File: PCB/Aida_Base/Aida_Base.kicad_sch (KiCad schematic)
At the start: 228 parts, among them J1 AudioJack4, J10 Conn_01x03_Pin, J11 Conn_01x04_Pin, J12 Conn_01x04_Pin, J13 Conn_01x04_Pin, J14 Conn_01x04_Pin, J15 Conn_01x04_Pin, J16 Conn_01x04_Pin, J17 Conn_02x02_Odd_Even, J18 Conn_02x02_Odd_Even, J19 Conn_01x04_Pin, J2 AudioJack4, J20 Conn_01x06_Pin, J21 Conn_01x06_Pin, J22 Conn_01x04_Pin, J3 USB_C_Receptacle_L, J4 USB_C_Receptacle_R, J5 Conn_01x02_Pin, J6 Conn_01x02_Pin, J7 Conn_01x05_Pin, J8 Conn_01x05_Pin, J9 Conn_01x03_Pin, Q1 BSS138, Q2 BSS138, SW1 BOOT, SW2 BOOT, SW3 RESET, SW4 RESET, U3 RP2040_L, U4 RP2040_R, U5 W25Q128JVS, U6 W25Q128JVS, U7 AP2112K-3.3, U8 AP2112K-3.3, Y1 12MHz, Y2 12MHz

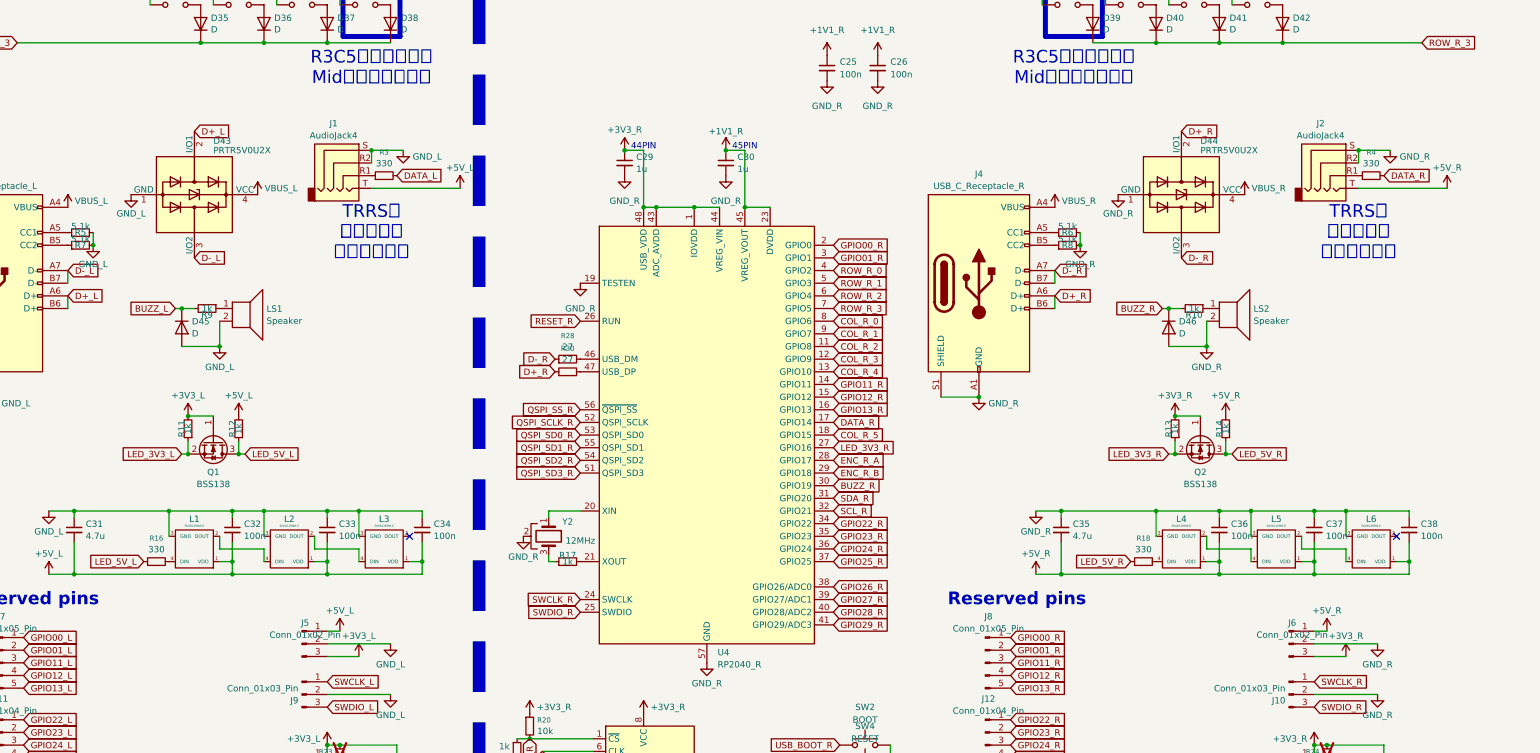
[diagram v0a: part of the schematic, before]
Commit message: 左手側配線。ほぼ完了。
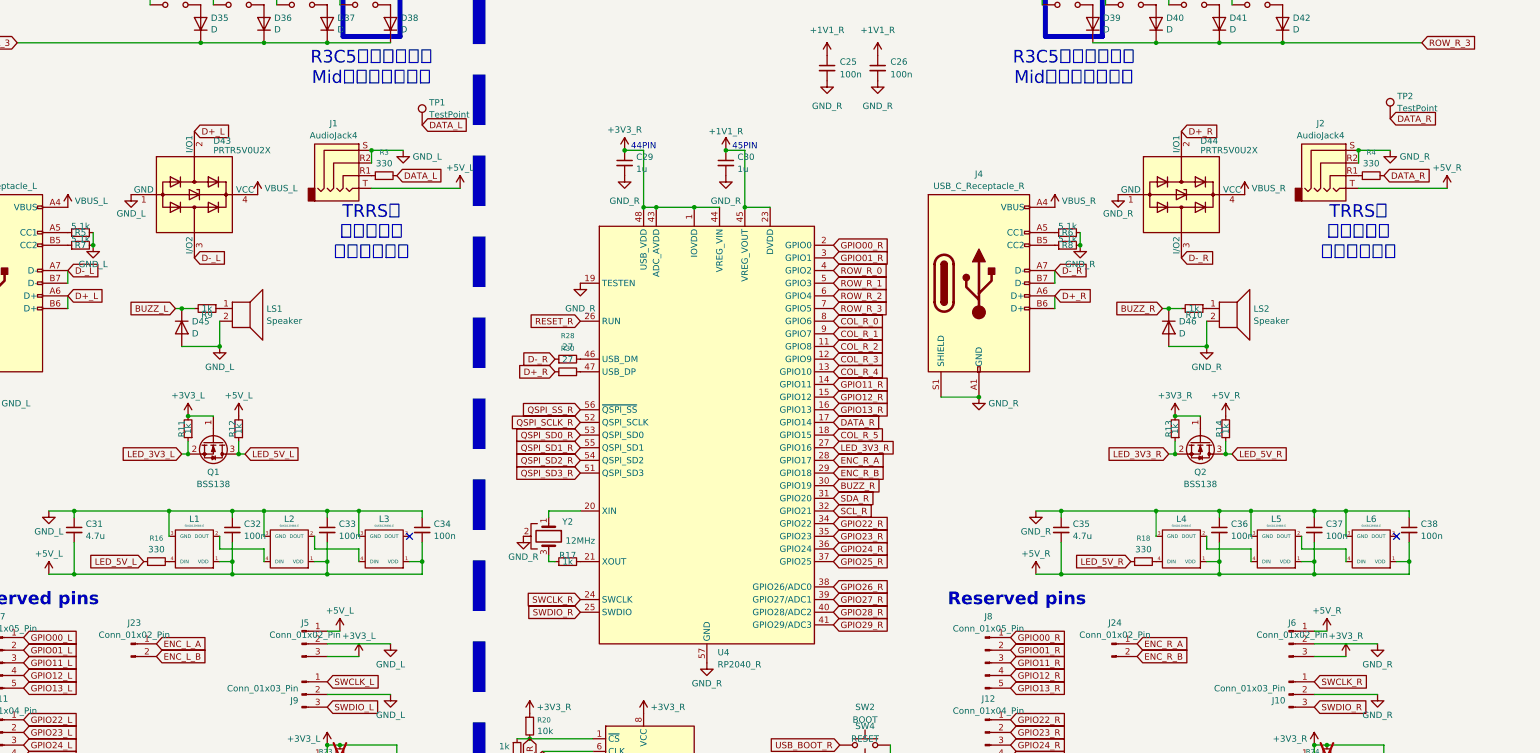
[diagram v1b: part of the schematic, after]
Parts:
- added J23, J24: Conn_01x02_Pin, Connector_PinHeader_2.00mm:PinHeader_1x02_P2.00mm_Vertical, symbol Connector:Conn_01x02_Pin
- added TP1, TP2: TestPoint, Connector_PinHeader_2.00mm:PinHeader_1x01_P2.00mm_Vertical, symbol Connector:TestPoint
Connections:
- net DATA_L: now also TP1.1
- net DATA_R: now also TP2.1
- net ENC_L_A: now also J23.1 (Pin_1)
- net ENC_L_B: now also J23.2 (Pin_2)
- net ENC_R_A: now also J24.1 (Pin_1)
- net ENC_R_B: now also J24.2 (Pin_2)

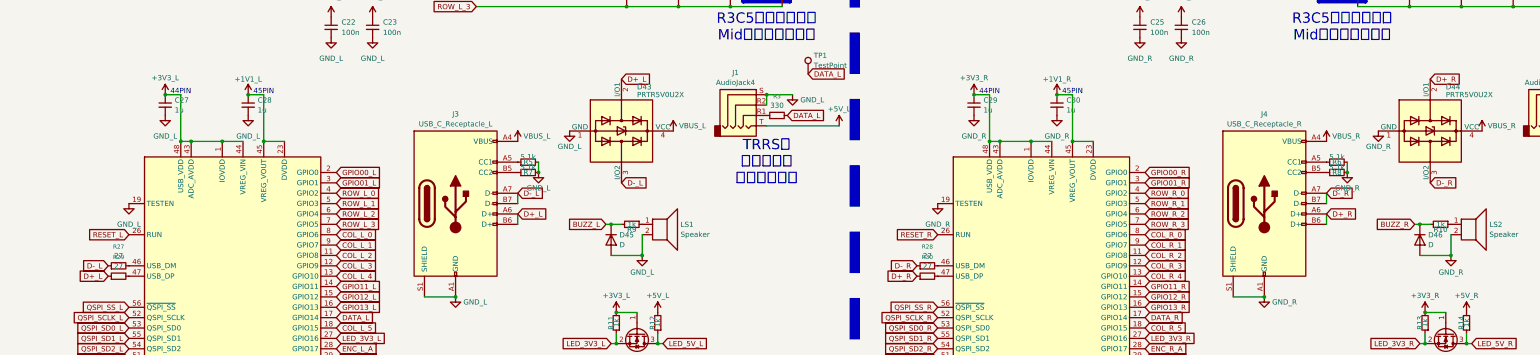
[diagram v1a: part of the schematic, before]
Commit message: ボトムプレートの穴あけ用に、左手側パーツ配置調整。
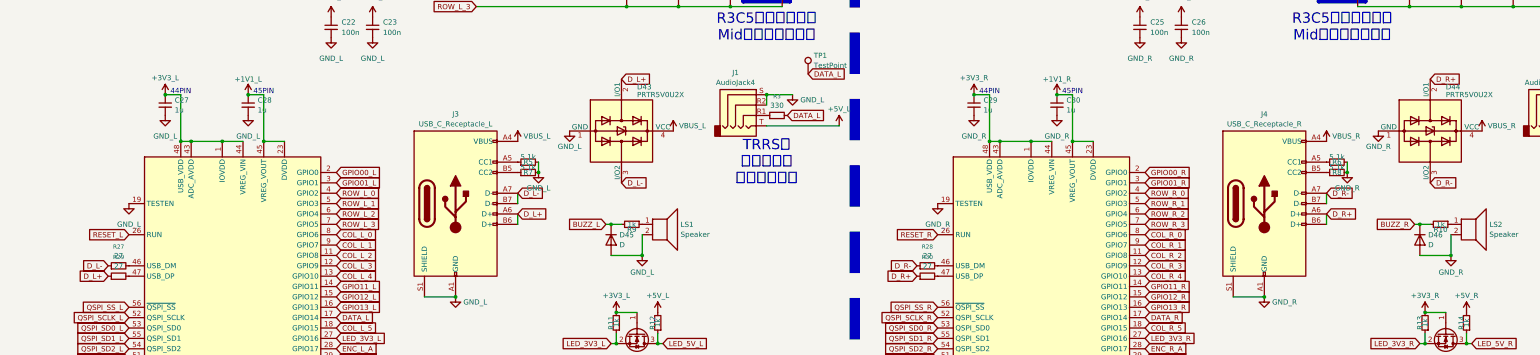
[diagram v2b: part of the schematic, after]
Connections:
- net D+_L renamed D_L+
- net D+_R renamed D_R+
- net D-_L renamed D_L-
- net D-_R renamed D_R-
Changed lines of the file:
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@@
 		)
 	)
-	(global_label "D+_R"
+	(global_label "D_R+"
 		(shape input)
 		(at 322.58 133.35 0)
@@
 		)
 	)
-	(global_label "D-_R"
+	(global_label "D_R-"
 		(shape input)
 		(at 322.58 128.27 0)
@@
 		)
 	)
-	(global_label "D-_L"
+	(global_label "D_L-"
 		(shape input)
 		(at 149.86 125.73 0)
@@
 		)
 	)
-	(global_label "D+_R"
+	(global_label "D_R+"
 		(shape input)
 		(at 347.98 100.33 0)
@@
 		)
 	)
-	(global_label "D-_L"
+	(global_label "D_L-"
 		(shape input)
 		(at 24.13 146.05 180)
@@
 		)
 	)
-	(global_label "D+_L"
+	(global_label "D_L+"
 		(shape input)
 		(at 149.86 100.33 0)
@@
 		)
 	)
-	(global_label "D+_L"
+	(global_label "D_L+"
 		(shape input)
 		(at 24.13 148.59 180)
@@
 		)
 	)
-	(global_label "D+_R"
+	(global_label "D_R+"
 		(shape input)
 		(at 222.25 148.59 180)
@@
 		)
 	)
-	(global_label "D-_R"
+	(global_label "D_R-"
 		(shape input)
 		(at 222.25 146.05 180)
@@
 		)
 	)
-	(global_label "D+_L"
+	(global_label "D_L+"
 		(shape input)
 		(at 124.46 133.35 0)
@@
 		)
 	)
-	(global_label "D-_L"
+	(global_label "D_L-"
 		(shape input)
 		(at 124.46 128.27 0)
@@
 		)
 	)
-	(global_label "D-_R"
+	(global_label "D_R-"
 		(shape input)
 		(at 347.98 125.73 0)

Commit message: 右手パーツ配置中。MCUまわりきびしい
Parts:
- D7: now not fitted
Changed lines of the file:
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@@
 		(exclude_from_sim no)
 		(in_bom yes)
-		(on_board yes)
-		(dnp no)
+		(on_board no)
+		(dnp yes)
 		(property "Reference" "D7"
 			(at 328.422 39.4716 90)

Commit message: 右手パーツ配置中
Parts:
- H_btm_L3, H_btm_L4, H_btm_L5, H_btm_L6: value MountingHole -> GND_L
- H_btm_R3, H_btm_R4, H_btm_R5, H_btm_R6: value MountingHole -> GND_R
- H_mid_L1, H_mid_L2: value MountingHole -> GND_L_to_Mid
- H_mid_R1, H_mid_R2: value MountingHole -> GND_R_to_Mid
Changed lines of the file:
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@@
 			)
 		)
-		(property "Value" "MountingHole"
+		(property "Value" "GND_R"
 			(at 217.17 276.733 0)
 			(effects
@@
 			)
 		)
-		(property "Value" "MountingHole"
+		(property "Value" "GND_L_to_Mid"
 			(at 73.66 267.843 0)
 			(effects
@@
 			)
 		)
-		(property "Value" "MountingHole"
+		(property "Value" "GND_L"
 			(at 41.91 276.733 0)
 			(effects
@@
 			)
 		)
-		(property "Value" "MountingHole"
+		(property "Value" "GND_L"
 			(at 21.59 271.653 0)
 			(effects
@@
 			)
 		)
-		(property "Value" "MountingHole"
+		(property "Value" "GND_R_to_Mid"
 			(at 271.78 267.843 0)
 			(effects
@@
 			)
 		)
-		(property "Value" "MountingHole"
+		(property "Value" "GND_L"
 			(at 19.05 276.733 0)
 			(effects
@@
 			)
 		)
-		(property "Value" "MountingHole"
+		(property "Value" "GND_R"
 			(at 237.49 271.653 0)
 			(effects
@@
 			)
 		)
-		(property "Value" "MountingHole"
+		(property "Value" "GND_R"
 			(at 240.03 276.733 0)
 			(effects
@@
 			)
 		)
-		(property "Value" "MountingHole"
+		(property "Value" "GND_L_to_Mid"
 			(at 90.17 267.843 0)
 			(effects
@@
 			)
 		)
-		(property "Value" "MountingHole"
+		(property "Value" "GND_L"
 			(at 39.37 271.653 0)
 			(effects
@@
 			)
 		)
-		(property "Value" "MountingHole"
+		(property "Value" "GND_R_to_Mid"
 			(at 288.29 267.843 0)
 			(effects
@@
 			)
 		)
-		(property "Value" "MountingHole"
+		(property "Value" "GND_R"
 			(at 219.71 271.653 0)
 			(effects

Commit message: ソケットの3Dモデルを、1.2ｍｍ厚のPCBに合わせて位置調整。
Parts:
- SW_-1, SW_/1, SW_<1, SW_>1, SW_A1, SW_B1, SW_BS1, SW_C1, SW_CMD_L1, SW_CMD_R1, SW_CTL1, SW_D1, SW_E1, SW_ENT1, SW_F1, SW_I1, SW_J1, SW_K1, SW_L1, SW_M1, SW_N1, SW_O1, SW_OPT_L1, SW_OPT_R1, SW_S1, SW_SPC1, SW_V1, SW_W1, SW_X1, SW_Z1: footprint Lib_Local:Kailh_socket_ChocV2 -> Lib_Local:Kailh_socket_ChocV2_for_T=1.2mmPCB
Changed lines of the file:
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@@
 			)
 		)
-		(property "Footprint" "Lib_Local:Kailh_socket_ChocV2"
+		(property "Footprint" "Lib_Local:Kailh_socket_ChocV2_for_T=1.2mmPCB"
 			(at 146.05 57.15 0)
 			(effects
@@
 			)
 		)
-		(property "Footprint" "Lib_Local:Kailh_socket_ChocV2"
+		(property "Footprint" "Lib_Local:Kailh_socket_ChocV2_for_T=1.2mmPCB"
 			(at 363.22 31.75 0)
 			(effects
@@
 			)
 		)
-		(property "Footprint" "Lib_Local:Kailh_socket_ChocV2"
+		(property "Footprint" "Lib_Local:Kailh_socket_ChocV2_for_T=1.2mmPCB"
 			(at 146.05 44.45 0)
 			(effects
@@
 			)
 		)
-		(property "Footprint" "Lib_Local:Kailh_socket_ChocV2"
+		(property "Footprint" "Lib_Local:Kailh_socket_ChocV2_for_T=1.2mmPCB"
 			(at 171.45 57.15 0)
 			(effects
@@
 			)
 		)
-		(property "Footprint" "Lib_Local:Kailh_socket_ChocV2"
+		(property "Footprint" "Lib_Local:Kailh_socket_ChocV2_for_T=1.2mmPCB"
 			(at 388.62 57.15 0)
 			(effects
@@
 			)
 		)
-		(property "Footprint" "Lib_Local:Kailh_socket_ChocV2"
+		(property "Footprint" "Lib_Local:Kailh_socket_ChocV2_for_T=1.2mmPCB"
 			(at 388.62 44.45 0)
 			(effects
@@
 			)
 		)
-		(property "Footprint" "Lib_Local:Kailh_socket_ChocV2"
+		(property "Footprint" "Lib_Local:Kailh_socket_ChocV2_for_T=1.2mmPCB"
 			(at 146.05 31.75 0)
 			(effects
@@
 			)
 		)
-		(property "Footprint" "Lib_Local:Kailh_socket_ChocV2"
+		(property "Footprint" "Lib_Local:Kailh_socket_ChocV2_for_T=1.2mmPCB"
 			(at 146.05 69.85 0)
 			(effects
@@
 			)
 		)
-		(property "Footprint" "Lib_Local:Kailh_socket_ChocV2"
+		(property "Footprint" "Lib_Local:Kailh_socket_ChocV2_for_T=1.2mmPCB"
 			(at 363.22 69.85 0)
 			(effects
@@
 			)
 		)
-		(property "Footprint" "Lib_Local:Kailh_socket_ChocV2"
+		(property "Footprint" "Lib_Local:Kailh_socket_ChocV2_for_T=1.2mmPCB"
 			(at 171.45 69.85 0)
 			(effects
@@
 			)
 		)
-		(property "Footprint" "Lib_Local:Kailh_socket_ChocV2"
+		(property "Footprint" "Lib_Local:Kailh_socket_ChocV2_for_T=1.2mmPCB"
 			(at 337.82 57.15 0)
 			(effects
@@
 			)
 		)
-		(property "Footprint" "Lib_Local:Kailh_socket_ChocV2"
+		(property "Footprint" "Lib_Local:Kailh_socket_ChocV2_for_T=1.2mmPCB"
 			(at 363.22 57.15 0)
 			(effects
@@
 			)
 		)
-		(property "Footprint" "Lib_Local:Kailh_socket_ChocV2"
+		(property "Footprint" "Lib_Local:Kailh_socket_ChocV2_for_T=1.2mmPCB"
 			(at 184.15 69.85 0)
 			(effects
@@
 			)
 		)
-		(property "Footprint" "Lib_Local:Kailh_socket_ChocV2"
+		(property "Footprint" "Lib_Local:Kailh_socket_ChocV2_for_T=1.2mmPCB"
 			(at 158.75 69.85 0)
 			(effects
@@
 			)
 		)
-		(property "Footprint" "Lib_Local:Kailh_socket_ChocV2"
+		(property "Footprint" "Lib_Local:Kailh_socket_ChocV2_for_T=1.2mmPCB"
 			(at 363.22 44.45 0)
 			(effects
@@
 			)
 		)
-		(property "Footprint" "Lib_Local:Kailh_socket_ChocV2"
+		(property "Footprint" "Lib_Local:Kailh_socket_ChocV2_for_T=1.2mmPCB"
 			(at 133.35 31.75 0)
 			(effects
@@
 			)
 		)
-		(property "Footprint" "Lib_Local:Kailh_socket_ChocV2"
+		(property "Footprint" "Lib_Local:Kailh_socket_ChocV2_for_T=1.2mmPCB"
 			(at 350.52 69.85 0)
 			(effects
@@
 			)
 		)
-		(property "Footprint" "Lib_Local:Kailh_socket_ChocV2"
+		(property "Footprint" "Lib_Local:Kailh_socket_ChocV2_for_T=1.2mmPCB"
 			(at 375.92 57.15 0)
 			(effects
@@
 			)
 		)
-		(property "Footprint" "Lib_Local:Kailh_socket_ChocV2"
+		(property "Footprint" "Lib_Local:Kailh_socket_ChocV2_for_T=1.2mmPCB"
 			(at 350.52 57.15 0)
 			(effects
@@
 			)
 		)
-		(property "Footprint" "Lib_Local:Kailh_socket_ChocV2"
+		(property "Footprint" "Lib_Local:Kailh_socket_ChocV2_for_T=1.2mmPCB"
 			(at 120.65 44.45 0)
 			(effects
@@
 			)
 		)
-		(property "Footprint" "Lib_Local:Kailh_socket_ChocV2"
+		(property "Footprint" "Lib_Local:Kailh_socket_ChocV2_for_T=1.2mmPCB"
 			(at 133.35 57.15 0)
 			(effects
@@
 			)
 		)
-		(property "Footprint" "Lib_Local:Kailh_socket_ChocV2"
+		(property "Footprint" "Lib_Local:Kailh_socket_ChocV2_for_T=1.2mmPCB"
 			(at 337.82 69.85 0)
 			(effects
@@
 			)
 		)
-		(property "Footprint" "Lib_Local:Kailh_socket_ChocV2"
+		(property "Footprint" "Lib_Local:Kailh_socket_ChocV2_for_T=1.2mmPCB"
 			(at 375.92 31.75 0)
 			(effects
@@
 			)
 		)
-		(property "Footprint" "Lib_Local:Kailh_socket_ChocV2"
+		(property "Footprint" "Lib_Local:Kailh_socket_ChocV2_for_T=1.2mmPCB"
 			(at 350.52 44.45 0)
 			(effects
@@
 			)
 		)
-		(property "Footprint" "Lib_Local:Kailh_socket_ChocV2"
+		(property "Footprint" "Lib_Local:Kailh_socket_ChocV2_for_T=1.2mmPCB"
 			(at 325.12 69.85 0)
 			(effects
@@
 			)
 		)
-		(property "Footprint" "Lib_Local:Kailh_socket_ChocV2"
+		(property "Footprint" "Lib_Local:Kailh_socket_ChocV2_for_T=1.2mmPCB"
 			(at 120.65 57.15 0)
 			(effects
@@
 			)
 		)
-		(property "Footprint" "Lib_Local:Kailh_socket_ChocV2"
+		(property "Footprint" "Lib_Local:Kailh_socket_ChocV2_for_T=1.2mmPCB"
 			(at 133.35 44.45 0)
 			(effects
@@
 			)
 		)
-		(property "Footprint" "Lib_Local:Kailh_socket_ChocV2"
+		(property "Footprint" "Lib_Local:Kailh_socket_ChocV2_for_T=1.2mmPCB"
 			(at 158.75 57.15 0)
 			(effects
@@
 			)
 		)
-		(property "Footprint" "Lib_Local:Kailh_socket_ChocV2"
+		(property "Footprint" "Lib_Local:Kailh_socket_ChocV2_for_T=1.2mmPCB"
 			(at 375.92 44.45 0)
 			(effects
@@
 			)
 		)
-		(property "Footprint" "Lib_Local:Kailh_socket_ChocV2"
+		(property "Footprint" "Lib_Local:Kailh_socket_ChocV2_for_T=1.2mmPCB"
 			(at 158.75 44.45 0)
 			(effects

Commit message: LEDのフットプリント変更。配線調整中。
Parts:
- L1, L2, L3, L4, L5, L6: footprint Lib_Local:YS-SK6812MINI-E_middle_hole_with_small_pad -> Lib_Local:YS-SK6812MINI-E_middle_hole_with_small_pad_NPTH
- SW1, SW2: value BOOT -> Boot
- SW3, SW4: value RESET -> Reset
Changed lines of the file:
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@@
 			)
 		)
-		(property "Footprint" "Lib_Local:YS-SK6812MINI-E_middle_hole_with_small_pad"
+		(property "Footprint" "Lib_Local:YS-SK6812MINI-E_middle_hole_with_small_pad_NPTH"
 			(at 149.86 184.15 0)
 			(effects
@@
 			)
 		)
-		(property "Footprint" "Lib_Local:YS-SK6812MINI-E_middle_hole_with_small_pad"
+		(property "Footprint" "Lib_Local:YS-SK6812MINI-E_middle_hole_with_small_pad_NPTH"
 			(at 187.96 184.15 0)
 			(effects
@@
 			)
 		)
-		(property "Value" "RESET"
+		(property "Value" "Reset"
 			(at 284.48 222.25 0)
 			(effects
@@
 			)
 		)
-		(property "Value" "RESET"
+		(property "Value" "Reset"
 			(at 86.36 222.25 0)
 			(effects
@@
 			)
 		)
-		(property "Footprint" "Lib_Local:YS-SK6812MINI-E_middle_hole_with_small_pad"
+		(property "Footprint" "Lib_Local:YS-SK6812MINI-E_middle_hole_with_small_pad_NPTH"
 			(at 347.98 184.15 0)
 			(effects
@@
 			)
 		)
-		(property "Footprint" "Lib_Local:YS-SK6812MINI-E_middle_hole_with_small_pad"
+		(property "Footprint" "Lib_Local:YS-SK6812MINI-E_middle_hole_with_small_pad_NPTH"
 			(at 168.91 184.15 0)
 			(effects
@@
 			)
 		)
-		(property "Footprint" "Lib_Local:YS-SK6812MINI-E_middle_hole_with_small_pad"
+		(property "Footprint" "Lib_Local:YS-SK6812MINI-E_middle_hole_with_small_pad_NPTH"
 			(at 386.08 184.15 0)
 			(effects
@@
 		(fields_autoplaced yes)
 		(property "Reference" "SW2"
-			(at 284.48 215.9 0)
+			(at 284.48 216.4545 0)
 			(effects
 				(font
@@
 			)
 		)
-		(property "Value" "BOOT"
-			(at 284.48 218.44 0)
+		(property "Value" "Boot"
+			(at 284.48 218.8788 0)
 			(effects
 				(font
@@
 			)
 		)
-		(property "Value" "BOOT"
+		(property "Value" "Boot"
 			(at 86.36 218.44 0)
 			(effects
@@
 			)
 		)
-		(property "Footprint" "Lib_Local:YS-SK6812MINI-E_middle_hole_with_small_pad"
+		(property "Footprint" "Lib_Local:YS-SK6812MINI-E_middle_hole_with_small_pad_NPTH"
 			(at 367.03 184.15 0)
 			(effects
